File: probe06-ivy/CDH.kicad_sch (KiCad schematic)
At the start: 45 parts, among them J2 Conn_Coaxial, Q1 S9014, U4 NEO-M8N, U5 24LC32, U6 BMP280

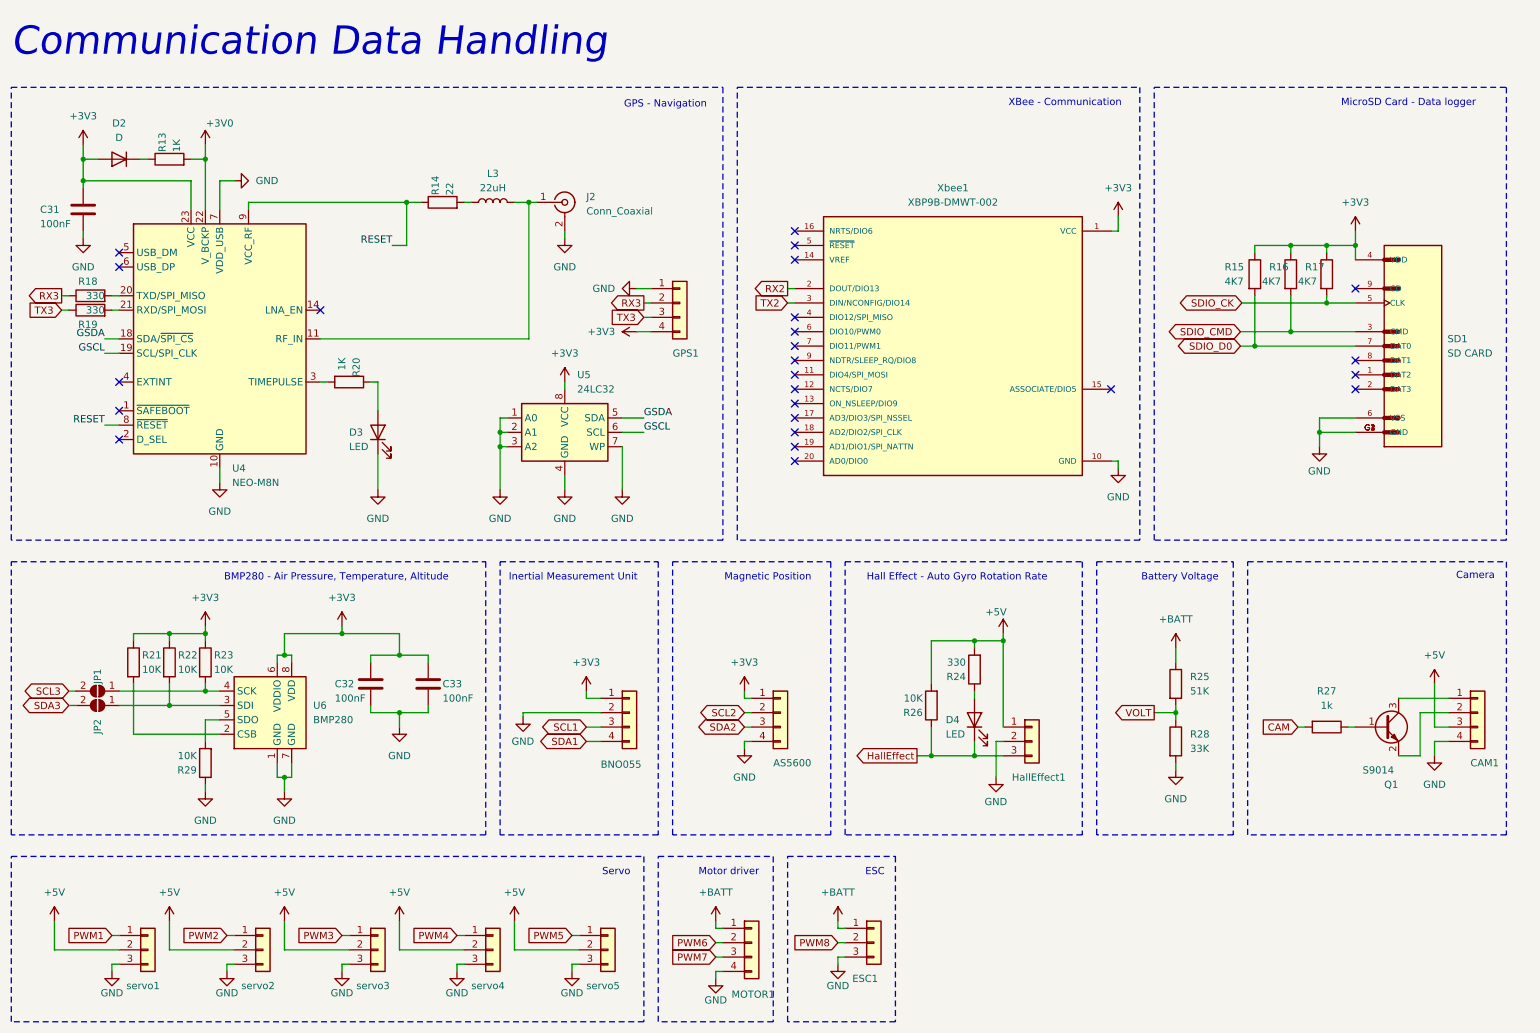
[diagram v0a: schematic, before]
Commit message: Routing Layout - add footprint to all components - pcb shape and dimension - component placement
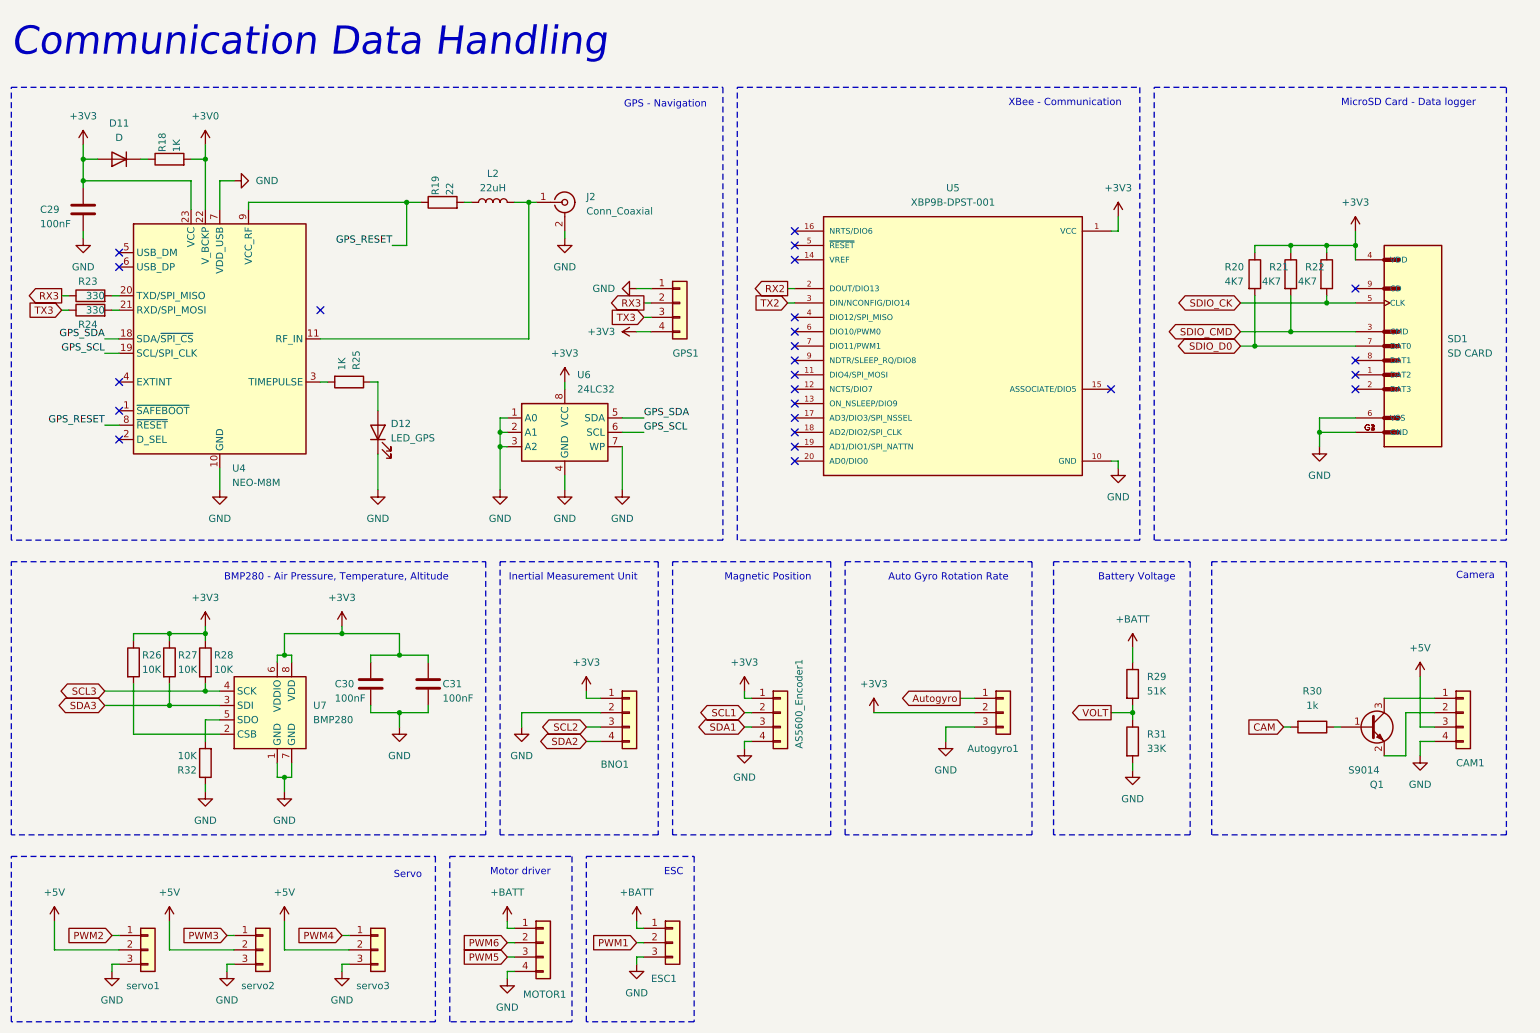
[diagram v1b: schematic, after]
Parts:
- removed D4: LED, LED_SMD:LED_0805_2012Metric, symbol Device:LED
- removed JP1, JP2: SolderJumper_2_Open, Jumper:SolderJumper-2_P1.3mm_Open_RoundedPad1.0x1.5mm, symbol Jumper:SolderJumper_2_Open
- removed R24: 330, Resistor_SMD:R_0805_2012Metric, symbol Device:R
- removed R26: 10K, Resistor_SMD:R_0805_2012Metric, symbol Device:R
- removed U4: NEO-M8N, RF_GPS:ublox_NEO, symbol RF_GPS:NEO-M8N
- removed Xbee1: XBP9B-DMWT-002, XBP9B-DMWT-002:DIP2200W51P200L3294H279Q20P, symbol XBP9B-DMWT-002:XBP9B-DMWT-002
- removed servo4, servo5: xx, Connector_JST:JST_EH_B3B-EH-A_1x03_P2.50mm_Vertical, symbol Connector_Generic:Conn_01x03
- added U4: NEO-M8M, RF_GPS:ublox_NEO, symbol RF_GPS:NEO-M8M
- added U5: XBP9B-DPST-001, XBP9B-DPST-001:DIP2200W51P200L3294H279Q20P, symbol XBP9B-DPST-001:XBP9B-DPST-001
- AS5600_Encoder1: renamed from AS5600; footprint Connector_JST:JST_EH_B4B-EH-A_1x04_P2.50mm_Vertical -> Connector_JST:JST_XH_B4B-XH-A_1x04_P2.50mm_Vertical
- Autogyro1: renamed from HallEffect1; footprint Connector_JST:JST_EH_B3B-EH-A_1x03_P2.50mm_Vertical -> Connector_JST:JST_XH_B3B-XH-A_1x03_P2.50mm_Vertical
- BNO1: renamed from BNO055; footprint Connector_JST:JST_EH_B4B-EH-A_1x04_P2.50mm_Vertical -> Connector_PinHeader_2.54mm:PinHeader_1x04_P2.54mm_Vertical
- C29: renamed from C31; footprint (none) -> Capacitor_SMD:C_0805_2012Metric
- C30: renamed from C32; footprint (none) -> Capacitor_SMD:C_0805_2012Metric
- C31: renamed from C33; footprint (none) -> Capacitor_SMD:C_0805_2012Metric
- CAM1, MOTOR1: footprint Connector_JST:JST_EH_B4B-EH-A_1x04_P2.50mm_Vertical -> Connector_JST:JST_XH_B4B-XH-A_1x04_P2.50mm_Vertical
- D11: renamed from D2; footprint (none) -> Diode_SMD:D_SOD-123
- D12: renamed from D3; value LED -> LED_GPS
- ESC1, servo1, servo2, servo3: footprint Connector_JST:JST_EH_B3B-EH-A_1x03_P2.50mm_Vertical -> Connector_JST:JST_XH_B3B-XH-A_1x03_P2.50mm_Vertical
- GPS1: footprint Connector_JST:JST_EH_B4B-EH-A_1x04_P2.50mm_Vertical -> Connector_PinHeader_2.54mm:PinHeader_1x04_P2.54mm_Vertical
- L2: renamed from L3; footprint (none) -> Inductor_SMD:L_0805_2012Metric
- U6: renamed from U5; footprint (none) -> Package_SO:TSSOP-8_4.4x3mm_P0.65mm
- renumbered R13 to R18, R14 to R19, R15 to R20, R16 to R21, R17 to R22, R18 to R23, R19 to R24, R20 to R25, R21 to R26, R22 to R27, R23 to R28, R25 to R29, R27 to R30, R28 to R31, R29 to R32, U6 to U7
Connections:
- net HallEffect is gone; now on net GND: Autogyro1.3 (Pin_3)
- net PWM7 is gone; now on net PWM5: MOTOR1.3 (Pin_3)
- net PWM8 is gone; now on net PWM1: ESC1.2 (Pin_2)
- net +3V0: now also U4.22 (V_BCKP)
- net +3V3: now also Autogyro1.2 (Pin_2), U4.23 (VCC), U5.1 (VCC)
- net +5V: no longer Autogyro1.1 (Pin_1)
- net GND: now also U4.10 (GND), U4.12 (GND), U4.13 (GND), U4.24 (GND), U4.7 (VDD_USB), U5.10 (GND); no longer Autogyro1.2 (Pin_2)
- net PWM1: no longer servo1.1 (Pin_1)
- net PWM2: now also servo1.1 (Pin_1); no longer servo2.1 (Pin_1)
- net PWM3: now also servo2.1 (Pin_1); no longer servo3.1 (Pin_1)
- net PWM4: now also servo3.1 (Pin_1)
- net RX2: now also U5.2 (DOUT/DIO13)
- net SCL1: now also AS5600_Encoder1.2 (Pin_2); no longer BNO1.3 (Pin_3)
- net SCL2: now also BNO1.3 (Pin_3); no longer AS5600_Encoder1.2 (Pin_2)
- net SCL3: now also R28.2, U7.4 (SCK)
- net SDA1: now also AS5600_Encoder1.3 (Pin_3); no longer BNO1.4 (Pin_4)
- net SDA2: now also BNO1.4 (Pin_4); no longer AS5600_Encoder1.3 (Pin_3)
- net SDA3: now also R27.2, U7.3 (SDI)
- net TX2: now also U5.3 (DIN/NCONFIG/DIO14)
- net at J2.1 (In), L2.2: now also U4.11 (RF_IN)
- net at R25.2: now also U4.3 (TIMEPULSE)
- net at R23.2: now also U4.20 (TXD/SPI_MISO)
- net at R24.2: now also U4.21 (RXD/SPI_MOSI)
- net GSCL renamed GPS_SCL
- net GPS_SCL: now also U4.19 (SCL/SPI_CLK)
- net GSDA renamed GPS_SDA
- net GPS_SDA: now also U4.18 (SDA/~{SPI_CS})
- net RESET renamed GPS_RESET
- net GPS_RESET: now also U4.8 (~{RESET}), U4.9 (VCC_RF)
- new net Autogyro: Autogyro1.1 (Pin_1)
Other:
- note added: "Auto Gyro Rotation Rate"
- note removed: "Hall Effect - Auto Gyro Rotation Rate"
- title: CanSat Avionics -> CanSat Avionics - Auto Gyro Descender
- moved on the sheet: Autogyro1, CAM1, ESC1, MOTOR1, Q1, R29, R30, R31

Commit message: Routing (2) - make the pcb edge cuts to suit mechanic requirements - route some components (power, usb debug, gps) progress 50%
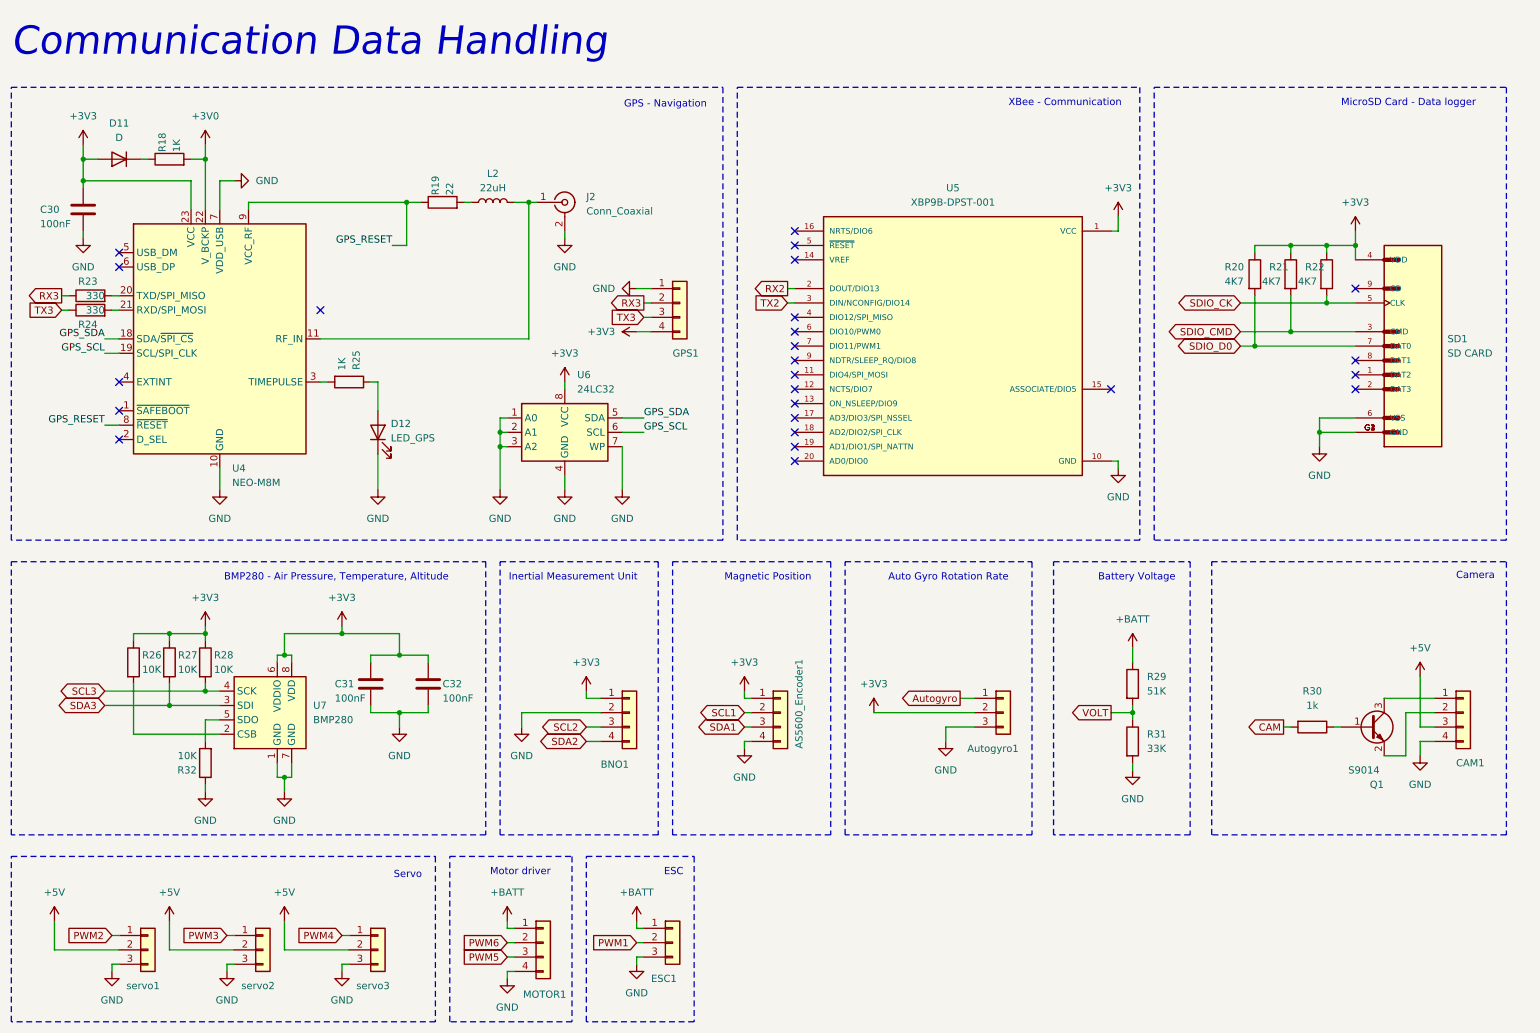
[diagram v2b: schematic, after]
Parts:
- C30: renamed from C29; footprint Capacitor_SMD:C_0805_2012Metric -> Capacitor_SMD:C_0603_1608Metric
- C31: renamed from C30; footprint Capacitor_SMD:C_0805_2012Metric -> Capacitor_SMD:C_0603_1608Metric
- C32: renamed from C31; footprint Capacitor_SMD:C_0805_2012Metric -> Capacitor_SMD:C_0603_1608Metric
- D12: footprint LED_SMD:LED_0805_2012Metric -> LED_SMD:LED_0603_1608Metric
- R18, R19, R20, R21, R22, R23, R24, R25, R26, R27, R28, R29, R30, R31, R32: footprint Resistor_SMD:R_0805_2012Metric -> Resistor_SMD:R_0603_1608Metric
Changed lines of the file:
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@@
 	)
 	(global_label "CAM"
-		(shape input)
+		(shape output)
 		(at 241.3 142.24 180)
 		(fields_autoplaced yes)
@@
 			)
 		)
-		(property "Footprint" "Resistor_SMD:R_0805_2012Metric"
+		(property "Footprint" "Resistor_SMD:R_0603_1608Metric"
 			(at 92.71 51.308 90)
 			(effects
@@
 			)
 		)
-		(property "Footprint" "Resistor_SMD:R_0805_2012Metric"
+		(property "Footprint" "Resistor_SMD:R_0603_1608Metric"
 			(at 212.852 144.78 90)
 			(effects
@@
 			)
 		)
-		(property "Footprint" "Resistor_SMD:R_0805_2012Metric"
+		(property "Footprint" "Resistor_SMD:R_0603_1608Metric"
 			(at 212.852 134.62 90)
 			(effects
@@
 			)
 		)
-		(property "Footprint" "Resistor_SMD:R_0805_2012Metric"
+		(property "Footprint" "Resistor_SMD:R_0603_1608Metric"
 			(at 76.2 79.502 90)
 			(effects
@@
 			)
 		)
-		(property "Footprint" "Resistor_SMD:R_0805_2012Metric"
+		(property "Footprint" "Resistor_SMD:R_0603_1608Metric"
 			(at 42.672 130.81 90)
 			(effects
@@
 			)
 		)
-		(property "Footprint" "Resistor_SMD:R_0805_2012Metric"
+		(property "Footprint" "Resistor_SMD:R_0603_1608Metric"
 			(at 234.442 62.23 90)
 			(effects
@@
 			)
 		)
-		(property "Footprint" "Resistor_SMD:R_0805_2012Metric"
+		(property "Footprint" "Resistor_SMD:R_0603_1608Metric"
 			(at 49.022 130.81 90)
 			(effects
@@
 			)
 		)
-		(property "Footprint" "Resistor_SMD:R_0805_2012Metric"
+		(property "Footprint" "Resistor_SMD:R_0603_1608Metric"
 			(at 247.142 62.23 90)
 			(effects
@@
 			)
 		)
-		(property "Footprint" "Resistor_SMD:R_0805_2012Metric"
+		(property "Footprint" "Resistor_SMD:R_0603_1608Metric"
 			(at 240.792 62.23 90)
 			(effects
@@
 			)
 		)
-		(property "Footprint" "Resistor_SMD:R_0805_2012Metric"
+		(property "Footprint" "Resistor_SMD:R_0603_1608Metric"
 			(at 44.45 43.688 90)
 			(effects
@@
 			)
 		)
-		(property "Footprint" "Resistor_SMD:R_0805_2012Metric"
+		(property "Footprint" "Resistor_SMD:R_0603_1608Metric"
 			(at 52.578 148.59 90)
 			(effects
@@
 		(on_board yes)
 		(dnp no)
-		(property "Reference" "C29"
+		(property "Reference" "C30"
 			(at 21.59 50.8 0)
 			(effects
@@
 			)
 		)
-		(property "Footprint" "Capacitor_SMD:C_0805_2012Metric"
+		(property "Footprint" "Capacitor_SMD:C_0603_1608Metric"
 			(at 30.1752 54.61 0)
 			(effects
@@
 			(project "probe06-ivy"
 				(path "/8ec4aa67-98d5-4482-bf96-6c1e71ad8a74/eceef58c-8170-45e6-b9eb-eb38a99a45f6"
-					(reference "C29")
+					(reference "C30")
 					(unit 1)
 				)
@@
 			)
 		)
-		(property "Footprint" "Resistor_SMD:R_0805_2012Metric"
+		(property "Footprint" "Resistor_SMD:R_0603_1608Metric"
 			(at 30.48 70.358 90)
 			(effects
@@
 			)
 		)
-		(property "Footprint" "Resistor_SMD:R_0805_2012Metric"
+		(property "Footprint" "Resistor_SMD:R_0603_1608Metric"
 			(at 246.38 140.462 90)
 			(effects
@@
 		(on_board yes)
 		(dnp no)
-		(property "Reference" "C31"
+		(property "Reference" "C32"
 			(at 92.71 134.62 0)
 			(effects
@@
 			)
 		)
-		(property "Footprint" "Capacitor_SMD:C_0805_2012Metric"
+		(property "Footprint" "Capacitor_SMD:C_0603_1608Metric"
 			(at 91.1352 138.43 0)
 			(effects
@@
 			(project "probe06-ivy"
 				(path "/8ec4aa67-98d5-4482-bf96-6c1e71ad8a74/eceef58c-8170-45e6-b9eb-eb38a99a45f6"
-					(reference "C31")
+					(reference "C32")
 					(unit 1)
 				)
@@
 			)
 		)
-		(property "Footprint" "Resistor_SMD:R_0805_2012Metric"
+		(property "Footprint" "Resistor_SMD:R_0603_1608Metric"
 			(at 30.48 67.818 90)
 			(effects
@@
 			)
 		)
-		(property "Footprint" "Resistor_SMD:R_0805_2012Metric"
+		(property "Footprint" "Resistor_SMD:R_0603_1608Metric"
 			(at 36.322 130.81 90)
 			(effects
@@
 			)
 		)
-		(property "Footprint" "LED_SMD:LED_0805_2012Metric"
+		(property "Footprint" "LED_SMD:LED_0603_1608Metric"
 			(at 81.28 90.17 0)
 			(effects
@@
 		(on_board yes)
 		(dnp no)
-		(property "Reference" "C30"
+		(property "Reference" "C31"
 			(at 73.66 134.62 0)
 			(effects
@@
 			)
 		)
-		(property "Footprint" "Capacitor_SMD:C_0805_2012Metric"
+		(property "Footprint" "Capacitor_SMD:C_0603_1608Metric"
 			(at 80.9752 138.43 0)
 			(effects
@@
 			(project "probe06-ivy"
 				(path "/8ec4aa67-98d5-4482-bf96-6c1e71ad8a74/eceef58c-8170-45e6-b9eb-eb38a99a45f6"
-					(reference "C30")
+					(reference "C31")
 					(unit 1)
 				)
